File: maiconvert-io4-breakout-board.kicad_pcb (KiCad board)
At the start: 2 copper layers, 170.8 x 114.6 mm, 90 parts, among them J1 CN3 - From IO4, J10 1P B7, J11 1P B8, J12 2P B1, J13 2P B2, J14 2P B3, J15 2P B4, J16 2P B5, J17 2P B6, J18 2P B7, J19 2P B8, J2 CN9 - From IO4, J20 1P SELECT BUTTON, J21 2P SELECT BUTTON, J22 12V input, J23 BILLBOARD LED L, J24 BILLBOARD LED R, J25 1P CODE READER LED, J26 2P CODE READER LED, J27 COIN METER, J28 COIN LOCKOUT, J29 CAMERA LED RED, J3 CN3 - To Harness, J30 CAMERA LED WARM, J31 TEST BUTTON, J32 COIN BUTTON, J33 SERVICE BUTTON, J4 1P B1, J5 1P B2, J6 1P B3, J7 1P B4, J8 1P B5, J9 1P B6, SW1 TEST, SW10 1P B5 BTN, SW11 1P B6 BTN, SW12 1P B7 BTN, SW13 1P B8 BTN, SW14 2P B1 BTN, SW15 2P B2 BTN, SW16 2P B3 BTN, SW17 2P B4 BTN, SW18 2P B5 BTN, SW19 2P B6 BTN, SW2 COIN, SW20 2P B7 BTN, SW21 2P B8 BTN, SW3 SERVICE, SW4 1P SELECT BTN, SW5 2P SELECT BTN, SW6 1P B1 BTN, SW7 1P B2 BTN, SW8 1P B3 BTN, SW9 1P B4 BTN

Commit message: Review and polish
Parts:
- removed D21: 1P CODE READER TEST LED, LED_RGB_Wurth:LED_RGB_Wurth_WL-SFTW_150352M173300
- removed D22: 2P CODE READER TEST LED, LED_RGB_Wurth:LED_RGB_Wurth_WL-SFTW_150352M173300
- added D3: 1P CODE READER TEST LED, LED_RGB_Wurth:LED_RGB_Wurth_WL-SFTW_150352M173300, F.Cu at (126.5, 56.9)
- added D4: 2P CODE READER TEST LED, LED_RGB_Wurth:LED_RGB_Wurth_WL-SFTW_150352M173300, F.Cu at (196.2, 56.8)
- added REF**: EVX needs to be connected to 5V for game to detect IO4, Connector_PinHeader_2.54mm:PinHeader_1x02_P2.54mm_Vertical, F.Cu at (94.7, 57.0)
- J3: value CN3 - To Harness -> CN3 - To Harness (Passthrough)
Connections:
- J1 pad 1: unconnected-(J1-Pin_1-Pad1) -> /EXV
- J1 pad 17: unconnected-(J1-Pin_17-Pad17) -> /NC 17
- J1 pad 18: unconnected-(J1-Pin_18-Pad18) -> /NC 18
- J1 pad 2: unconnected-(J1-Pin_2-Pad2) -> /EXV
- J1 pad 23: unconnected-(J1-Pin_23-Pad23) -> /NC 23
- J1 pad 24: unconnected-(J1-Pin_24-Pad24) -> /NC 24
- J1 pad 25: unconnected-(J1-Pin_25-Pad25) -> /NC 25
- J1 pad 28: unconnected-(J1-Pin_28-Pad28) -> /NC 28
- J1 pad 42: unconnected-(J1-Pin_42-Pad42) -> /NC 42
- J1 pad 44: unconnected-(J1-Pin_44-Pad44) -> /NC 44
- J1 pad 46: unconnected-(J1-Pin_46-Pad46) -> /NC 46
- J1 pad 47: unconnected-(J1-Pin_47-Pad47) -> /NC 47
- J1 pad 48: unconnected-(J1-Pin_48-Pad48) -> /NC 48
- J1 pad 50: unconnected-(J1-Pin_50-Pad50) -> /NC 50
- J1 pad 54: unconnected-(J1-Pin_54-Pad54) -> /NC 54
- J3 pad 1: unconnected-(J3-Pin_1-Pad1) -> /EXV
- J3 pad 17: unconnected-(J3-Pin_17-Pad17) -> /NC 17
- J3 pad 18: unconnected-(J3-Pin_18-Pad18) -> /NC 18
- J3 pad 2: unconnected-(J3-Pin_2-Pad2) -> /EXV
- J3 pad 23: unconnected-(J3-Pin_23-Pad23) -> /NC 23
- J3 pad 24: unconnected-(J3-Pin_24-Pad24) -> /NC 24
- J3 pad 25: unconnected-(J3-Pin_25-Pad25) -> /NC 25
- J3 pad 28: unconnected-(J3-Pin_28-Pad28) -> /NC 28
- J3 pad 42: unconnected-(J3-Pin_42-Pad42) -> /NC 42
- J3 pad 44: unconnected-(J3-Pin_44-Pad44) -> /NC 44
- J3 pad 46: unconnected-(J3-Pin_46-Pad46) -> /NC 46
- J3 pad 47: unconnected-(J3-Pin_47-Pad47) -> /NC 47
- J3 pad 48: unconnected-(J3-Pin_48-Pad48) -> /NC 48
- J3 pad 50: unconnected-(J3-Pin_50-Pad50) -> /NC 50
- J3 pad 54: unconnected-(J3-Pin_54-Pad54) -> /NC 54
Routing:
- net /EXV: track 0.00 -> 26.7 mm
- net /NC 24: track 0.00 -> 12.7 mm
- net /NC 18: track 0.00 -> 12.6 mm
- net /NC 23: track 0.00 -> 12.5 mm
- net /NC 48: track 0.00 -> 12.5 mm
- net /NC 28: track 0.00 -> 12.5 mm
- net /NC 54: track 0.00 -> 12.5 mm
- net /NC 46: track 0.00 -> 12.5 mm
- net /NC 42: track 0.00 -> 12.5 mm
- net /NC 17: track 0.00 -> 12.5 mm
- net /NC 50: track 0.00 -> 12.5 mm
- net /NC 47: track 0.00 -> 12.5 mm
- net /NC 44: track 0.00 -> 12.5 mm
- net /NC 25: track 0.00 -> 12.5 mm
- net /SERVICE SW: track 119.4 -> 121.0 mm
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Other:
- board text added: "12V"
- board text added: "5V"
- board text added: "B"
- board text added: "EXV"
- board text added: "EXV needs to be connected to 5V or the game won't see the IO4"
- board text added: "For 1P 1-8, if no button is connected, put a jumper on pin 2 and 3, or tactile switches will no work"
- board text added: "For 2P 1-8, if no button is connected, put a jumper on pin 2 and 3, or tactile switches will no work"
- board text added: "G"
- board text added: "GND"
- board text added: "R"
- board text added: "common cathode from IO4 for R G and B"
- board text added: "Ω"

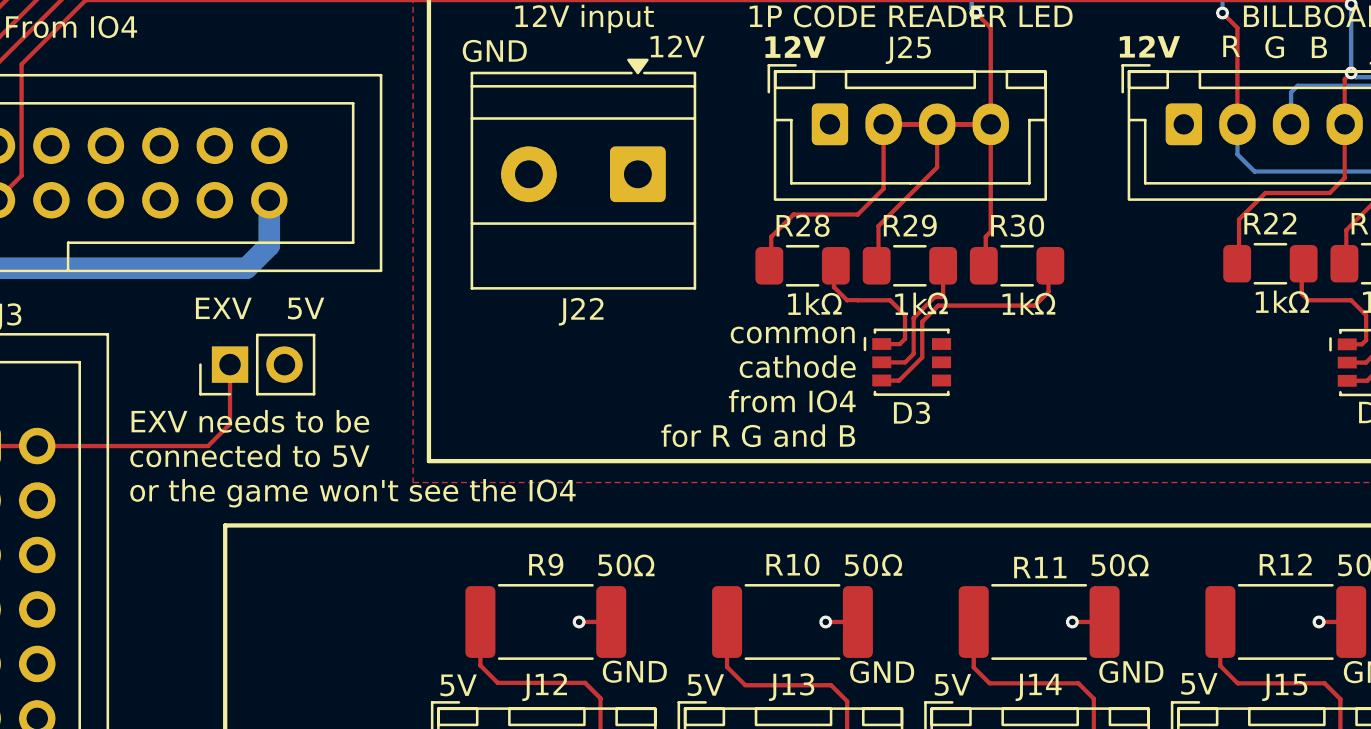
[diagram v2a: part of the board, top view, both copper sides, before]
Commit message: Add 12v input protaction
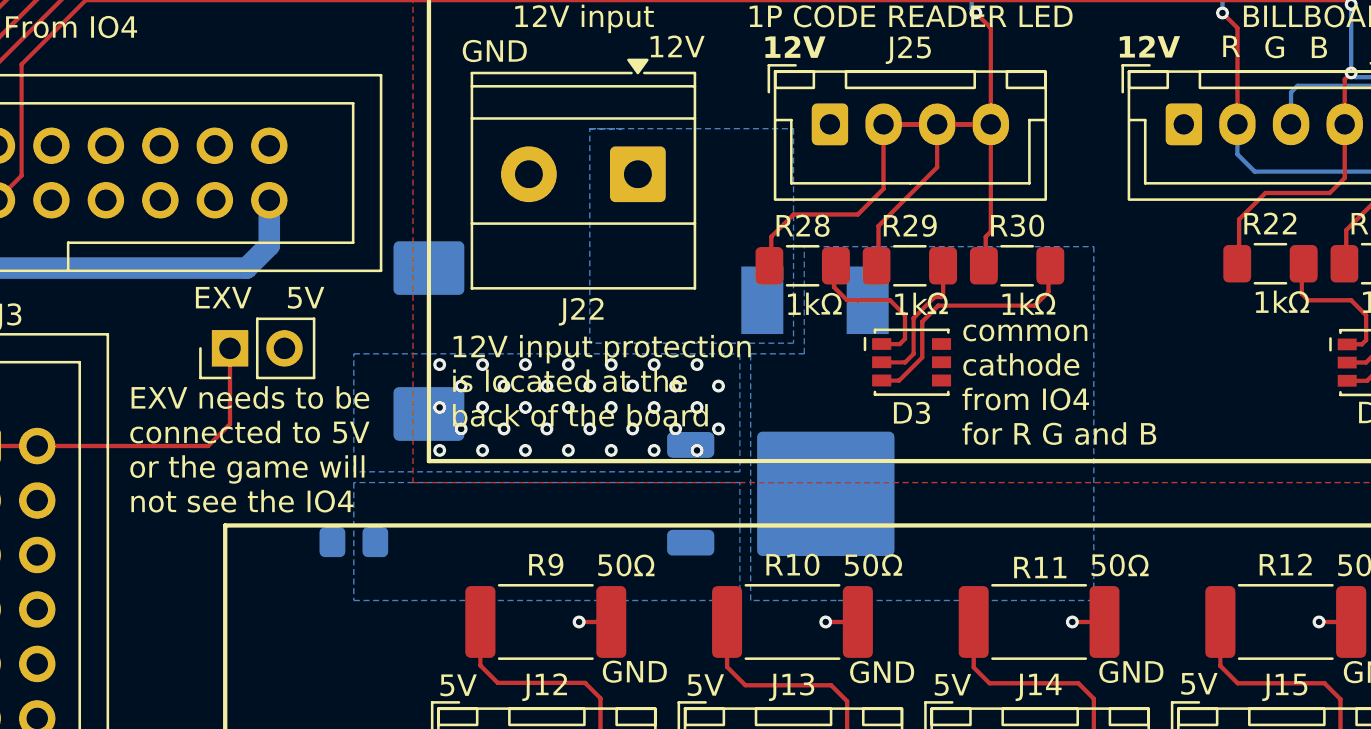
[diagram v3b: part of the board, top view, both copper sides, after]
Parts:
- added D5: SMCJ15A, Diode_SMD:D_SMC, B.Cu at (104.0, 55.9)
- added F1: 15A, Fuse:Fuse_Littelfuse-NANO2-451_453, B.Cu at (122.0, 54.0)
- added Q1: DMP3010LK3-13, Package_TO_SOT_SMD:TO-252-2, B.Cu at (121.2, 63.0)
- added R17: 100k, Resistor_SMD:R_0805_2012Metric_Pad1.20x1.40mm_HandSolder, B.Cu at (100.5, 65.3)
- moved REF** 0.76 mm to (94.7, 56.2)
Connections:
- J22 pad 1: +12V -> Net-(J22-Pin_1)
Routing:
- net +12V: vias 0 -> 35
- added copper zone on B.Cu, net +12V
- added copper zone on B.Cu, net Net-(J22-Pin_1)
- added copper zone on B.Cu, net Net-(Q1-D)
- added copper zone on B.Cu, net Net-(Q1-G)
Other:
- board text added: "12V input protection is located at the back of the board"
- board text added: "EXV needs to be connected to 5V or the game will not see the IO4"
- board text removed: "EXV needs to be connected to 5V or the game won't see the IO4"

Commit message: Fix layers issues
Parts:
- REF**: value EVX needs to be connected to 5V for game to detect IO4 -> EXV needs to be connected to 5V for game to detect IO4
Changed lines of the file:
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@@
 		(property "Reference" "REF**"
 			(at 0 -2.38 90)
-			(layer "F.SilkS")
-			(hide yes)
-			(effects
-				(font
-					(size 1 1)
-					(thickness 0.15)
-				)
-			)
-		)
-		(property "Value" "EVX needs to be connected to 5V for game to detect IO4"
+			(layer "Cmts.User")
+			(hide yes)
+			(effects
+				(font
+					(size 1 1)
+					(thickness 0.15)
+				)
+			)
+		)
+		(property "Value" "EXV needs to be connected to 5V for game to detect IO4"
 			(at -0.5 15.04 180)
-			(layer "F.SilkS")
+			(layer "Cmts.User")
 			(hide yes)
 			(effects
@@
 		(property "Reference" "REF**"
 			(at 0 4.15 180)
-			(layer "B.SilkS")
+			(layer "Cmts.User")
 			(hide yes)
 			(effects
@@
 		(property "Reference" "REF**"
 			(at 0 4.15 180)
-			(layer "B.SilkS")
+			(layer "Cmts.User")
 			(hide yes)
 			(effects
@@
 		(property "Reference" "REF**"
 			(at 0 4.15 180)
-			(layer "B.SilkS")
+			(layer "Cmts.User")
 			(hide yes)
 			(effects
@@
 		(property "Reference" "REF**"
 			(at 0 4.15 180)
-			(layer "B.SilkS")
-			(hide yes)
-			(effects
+			(layer "Cmts.User")
+			(hide yes)
+			(effects

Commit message: Final touche, add board title and signature
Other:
- board text added: "Irresponsibly made by Yttris - 2026"
- board text added: "maiConvert-IO4 : Breakout board"
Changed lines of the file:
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@@
 			(layer "F.Mask"
 				(type "Top Solder Mask")
-				(color "Green")
+				(color "Purple")
 				(thickness 0.01)
 			)
@@
 			(layer "B.Mask"
 				(type "Bottom Solder Mask")
-				(color "Green")
+				(color "Purple")
 				(thickness 0.01)
 			)
@@
 				(type "Bottom Silk Screen")
 			)
-			(copper_finish "HASL lead-free")
+			(copper_finish "User defined")
 			(dielectric_constraints no)
 		)
@@
 		)
 		(embedded_fonts no)
-		(model "${KICAD9_3DMODEL_DIR}/Fuse.3dshapes/Fuse_Littelfuse-NANO2-451_453.step"
+		(model "${KIPRJMOD}/libraries/Fuse.3dshapes/Fuse_Littelfuse-NANO2-451_453.step"
 			(offset
 				(xyz 0 0 0)
@@
 		(layer "Edge.Cuts")
 	)
+	(gr_text "maiConvert-IO4 : Breakout board"
+		(at 69 38.5 0)
+		(layer "F.SilkS")
+		(effects
+			(font
+				(size 2 2)
+				(thickness 0.3)
+			)
+			(justify left bottom)
+		)
+	)
 	(gr_text "Ω"
 		(at 136.54 94.04 0)
@@
 			)
 			(justify left bottom)
+		)
+	)
+	(gr_text "Irresponsibly made by Yttris - 2026"
+		(at 163 147 0)
+		(layer "F.SilkS")
+		(effects
+			(font
+				(size 2 2)
+				(thickness 0.3)
+			)
+			(justify left bottom)

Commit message: Update PCB appearance
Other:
- board text added: "This board is freely available online"

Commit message: Add onboard bridge pins to allow user to specify harness structure
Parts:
- removed the REF** at (94.7, 56.2)
- added J34: EXV-5V Jumper, Connector_PinHeader_2.54mm:PinHeader_1x02_P2.54mm_Vertical, F.Cu at (94.7, 56.2)
- added J35: Pin 51 Jumper, Connector_PinHeader_2.54mm:PinHeader_1x03_P2.54mm_Vertical, F.Cu at (81.9, 143.5)
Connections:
- J3 pad 51: /BILLBOARD LED L RED -> /Passthrough pin 51
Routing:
- net /Passthrough pin 51: track 0.00 -> 28.5 mm, vias 0 -> 1
- net /COIN LOCKOUT: track 155.9 -> 170.5 mm, vias 1 -> 3
- net /BILLBOARD LED L RED: track 265.0 -> 267.6 mm, vias 2 -> 4
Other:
- board text added: "DX"
- board text added: "FiNALE"
- board text added: "J3 Harness compatibility mode"
